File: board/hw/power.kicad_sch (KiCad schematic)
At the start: 1 part, among them U2 LM78L05_SO8

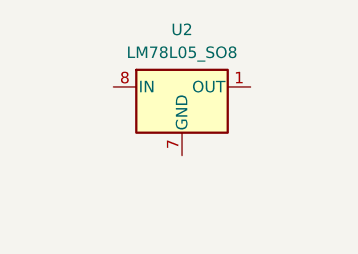
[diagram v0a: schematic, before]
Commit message: added cristal oscillator with capacitors, and 3.3V LDO voltage regulator
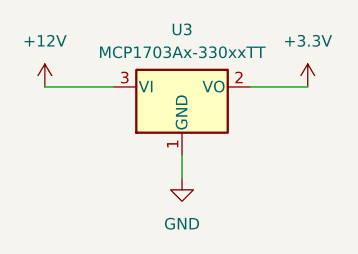
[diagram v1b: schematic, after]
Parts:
- removed U2: LM78L05_SO8, Package_SO:SOIC-8_3.9x4.9mm_P1.27mm, symbol Regulator_Linear:LM78L05_SO8
- added U3: MCP1703Ax-330xxTT, Package_TO_SOT_SMD:SOT-23, symbol Regulator_Linear:MCP1703Ax-330xxTT
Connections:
- new net +12V: U3.3 (VI)
- new net +3.3V: U3.2 (VO)
- new net GND: U3.1 (GND)
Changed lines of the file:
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@@
 (kicad_sch (version 20230121) (generator eeschema)
   (paper "A4")
-  (symbol (lib_id "Regulator_Linear:LM78L05_SO8") (at 77.47 62.23 0) (unit 1)
+  (wire (pts (xy 77.47 69.85) (xy 77.47 72.39))
+    (stroke (width 0) (type default))
+  )
+  (wire (pts (xy 62.23 62.23) (xy 69.85 62.23))
+    (stroke (width 0) (type default))
+  )
+  (wire (pts (xy 85.09 62.23) (xy 91.44 62.23))
+    (stroke (width 0) (type default))
+  )
+  (symbol (lib_id "power:+3.3V") (at 91.44 62.23 0) (unit 1)
     (in_bom yes) (on_board yes) (dnp no) (fields_autoplaced)
-    (property "Reference" "U2" (at 77.47 55.88 0)
+    (property "Reference" "#PWR01" (at 91.44 66.04 0)
+      (effects (font (size 1.27 1.27)) hide)
+    )
+    (property "Value" "+3.3V" (at 91.44 57.15 0)
       (effects (font (size 1.27 1.27)))
     )
-    (property "Value" "LM78L05_SO8" (at 77.47 58.42 0)
-      (effects (font (size 1.27 1.27)))
-    )
-    (property "Footprint" "Package_SO:SOIC-8_3.9x4.9mm_P1.27mm" (at 80.01 57.15 0)
-      (effects (font (size 1.27 1.27) italic) hide)
-    )
-    (property "Datasheet" "https://www.onsemi.com/pub/Collateral/MC78L06A-D.pdf" (at 82.55 62.23 0)
+    (property "Footprint" "" (at 91.44 62.23 0)
       (effects (font (size 1.27 1.27)) hide)
     )
-    (pin "5")
-    (pin "4")
-    (pin "8")
-    (pin "2")
-    (pin "3")
+    (property "Datasheet" "" (at 91.44 62.23 0)
+      (effects (font (size 1.27 1.27)) hide)
+    )
     (pin "1")
-    (pin "6")
-    (pin "7")
     (instances
       (project "yals"
         (path "/920838ab-42d6-4f6a-a4ed-bf4606dd42d5/2a492668-7486-4f4c-801e-63d1e5f9110f"
-          (reference "U2") (unit 1)
+          (reference "#PWR01") (unit 1)
         )
       )
+    )
+  )
+  (symbol (lib_id "power:+12V") (at 62.23 62.23 0) (unit 1)
+    (in_bom yes) (on_board yes) (dnp no) (fields_autoplaced)
+    (property "Reference" "#PWR03" (at 62.23 66.04 0)
+      (effects (font (size 1.27 1.27)) hide)
+    )
+    (property "Value" "+12V" (at 62.23 57.15 0)
+      (effects (font (size 1.27 1.27)))
+    )
+    (property "Footprint" "" (at 62.23 62.23 0)
+      (effects (font (size 1.27 1.27)) hide)
+    )
+    (property "Datasheet" "" (at 62.23 62.23 0)
+      (effects (font (size 1.27 1.27)) hide)
+    )
+    (pin "1")
+    (instances
+      (project "yals"
+        (path "/920838ab-42d6-4f6a-a4ed-bf4606dd42d5/2a492668-7486-4f4c-801e-63d1e5f9110f"
+          (reference "#PWR03") (unit 1)
+        )
+      )
+    )
+  )
+  (symbol (lib_id "power:GND") (at 77.47 72.39 0) (unit 1)
+    (in_bom yes) (on_board yes) (dnp no) (fields_autoplaced)
+    (property "Reference" "#PWR02" (at 77.47 78.74 0)
+      (effects (font (size 1.27 1.27)) hide)
+    )
+    (property "Value" "GND" (at 77.47 77.47 0)
+      (effects (font (size 1.27 1.27)))
+    )
+    (property "Footprint" "" (at 77.47 72.39 0)
+      (effects (font (size 1.27 1.27)) hide)
+    )
+    (property "Datasheet" "" (at 77.47 72.39 0)
+      (effects (font (size 1.27 1.27)) hide)
+    )
+    (pin "1")
+    (instances
+      (project "yals"
+        (path "/920838ab-42d6-4f6a-a4ed-bf4606dd42d5/2a492668-7486-4f4c-801e-63d1e5f9110f"
+          (reference "#PWR02") (unit 1)
+        )
+      )
+    )
+  )
+  (symbol (lib_id "Regulator_Linear:MCP1703Ax-330xxTT") (at 77.47 62.23 0) (unit 1)
+    (in_bom yes) (on_board yes) (dnp no) (fields_autoplaced)
+    (property "Reference" "U3" (at 77.47 55.88 0)
+      (effects (font (size 1.27 1.27)))
+    )
+    (property "Value" "MCP1703Ax-330xxTT" (at 77.47 58.42 0)
+      (effects (font (size 1.27 1.27)))
+    )
+    (property "Footprint" "Package_TO_SOT_SMD:SOT-23" (at 77.47 57.15 0)
+      (effects (font (size 1.27 1.27)) hide)
+    )
+    (property "Datasheet" "http://ww1.microchip.com/downloads/en/DeviceDoc/20005122B.pdf" (at 77.47 63.5 0)
+      (effects (font (size 1.27 1.27)) hide)
+    )
+    (pin "3")
+    (pin "1")
+    (pin "2")
+    (instances
+      (project "yals"
+        (path "/920838ab-42d6-4f6a-a4ed-bf4606dd42d5/2a492668-7486-4f4c-801e-63d1e5f9110f"
+          (reference "U3") (unit 1)
+        )
+      )

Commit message: power block is almost ready
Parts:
- added C3, C6: 100nF, Capacitor_SMD:C_1206_3216Metric, symbol Device:C
- added C4: 4.7uF, Capacitor_SMD:CP_Elec_5x4.5, symbol Device:C_Polarized
- added C5: 10uF, Capacitor_SMD:CP_Elec_5x4.5, symbol Device:C_Polarized
- added D1: TS418C, Diode_SMD:D_0603_1608Metric, symbol Diode:SM513
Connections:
- net +12V: now also D1.2 (A); no longer U3.3 (VI)
- net +3.3V: now also C3.1, C4.1
- net GND: now also C3.2, C4.2, C5.2, C6.2
- new net: C5.1, C6.1, D1.1 (K), U3.3 (VI)

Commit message: added board's outer dimensions, placed some more components and added missing power supply slot
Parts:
- added J4: power, Connector_PinHeader_2.54mm:PinHeader_1x02_P2.54mm_Vertical, symbol Connector_Generic:Conn_01x02
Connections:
- net +12V: now also J4.1 (Pin_1)
- net GND: now also J4.2 (Pin_2)
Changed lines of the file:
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@@
     (stroke (width 0) (type default))
   )
+  (symbol (lib_id "power:+12V") (at 38.735 100.33 0) (unit 1)
+    (in_bom yes) (on_board yes) (dnp no) (fields_autoplaced)
+    (property "Reference" "#PWR050" (at 38.735 104.14 0)
+      (effects (font (size 1.27 1.27)) hide)
+    )
+    (property "Value" "+12V" (at 38.735 95.25 0)
+      (effects (font (size 1.27 1.27)))
+    )
+    (property "Footprint" "" (at 38.735 100.33 0)
+      (effects (font (size 1.27 1.27)) hide)
+    )
+    (property "Datasheet" "" (at 38.735 100.33 0)
+      (effects (font (size 1.27 1.27)) hide)
+    )
+    (pin "1")
+    (instances
+      (project "yals"
+        (path "/920838ab-42d6-4f6a-a4ed-bf4606dd42d5/2a492668-7486-4f4c-801e-63d1e5f9110f"
+          (reference "#PWR050") (unit 1)
+        )
+      )
+    )
+  )
   (symbol (lib_id "Device:C") (at 87.63 66.04 0) (unit 1)
     (in_bom yes) (on_board yes) (dnp no) (fields_autoplaced)
@@
     )
   )
+  (symbol (lib_id "Connector_Generic:Conn_01x02") (at 33.655 100.33 0) (mirror y) (unit 1)
+    (in_bom yes) (on_board yes) (dnp no)
+    (property "Reference" "J4" (at 31.115 100.33 0)
+      (effects (font (size 1.27 1.27)) (justify left))
+    )
+    (property "Value" "power" (at 31.115 102.87 0)
+      (effects (font (size 1.27 1.27)) (justify left))
+    )
+    (property "Footprint" "Connector_PinHeader_2.54mm:PinHeader_1x02_P2.54mm_Vertical" (at 33.655 100.33 0)
+      (effects (font (size 1.27 1.27)) hide)
+    )
+    (property "Datasheet" "~" (at 33.655 100.33 0)
+      (effects (font (size 1.27 1.27)) hide)
+    )
+    (pin "2")
+    (pin "1")
+    (instances
+      (project "yals"
+        (path "/920838ab-42d6-4f6a-a4ed-bf4606dd42d5/2a492668-7486-4f4c-801e-63d1e5f9110f"
+          (reference "J4") (unit 1)
+        )
+      )
+    )
+  )
   (symbol (lib_id "Device:C_Polarized") (at 100.33 66.04 0) (unit 1)
     (in_bom yes) (on_board yes) (dnp no)
@@
         )
       )
+    )
+  )
+  (symbol (lib_id "power:GND") (at 38.735 102.87 0) (unit 1)
+    (in_bom yes) (on_board yes) (dnp no) (fields_autoplaced)
+    (property "Reference" "#PWR051" (at 38.735 109.22 0)
+      (effects (font (size 1.27 1.27)) hide)
+    )
+    (property "Value" "GND" (at 38.735 107.95 0)
+      (effects (font (size 1.27 1.27)))
+    )
+    (property "Footprint" "" (at 38.735 102.87 0)
+      (effects (font (size 1.27 1.27)) hide)
+    )
+    (property "Datasheet" "" (at 38.735 102.87 0)
+      (effects (font (size 1.27 1.27)) hide)
+    )
+    (pin "1")
+    (instances
+      (project "yals"
+        (path "/920838ab-42d6-4f6a-a4ed-bf4606dd42d5/2a492668-7486-4f4c-801e-63d1e5f9110f"
+          (reference "#PWR051") (unit 1)
+        )
+      )
